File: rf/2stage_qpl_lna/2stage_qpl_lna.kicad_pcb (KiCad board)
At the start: 6 copper layers, 42 x 25 mm, 26 parts, among them J1 SMA, J2 EXT_PWR, J3 SMA, U1 QPL9547, U2 QPL9547, X1 SAW, X2 SAW

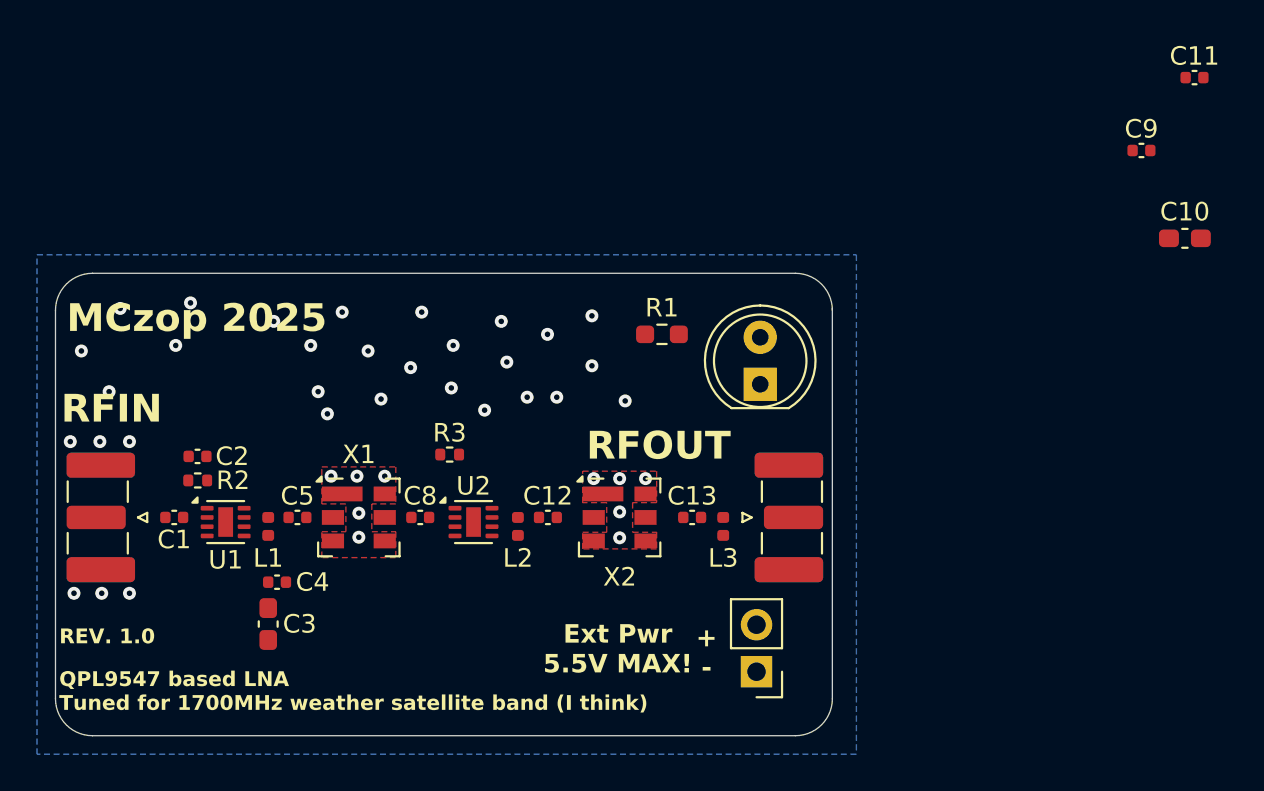
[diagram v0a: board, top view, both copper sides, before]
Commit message: Update QPL based LNA
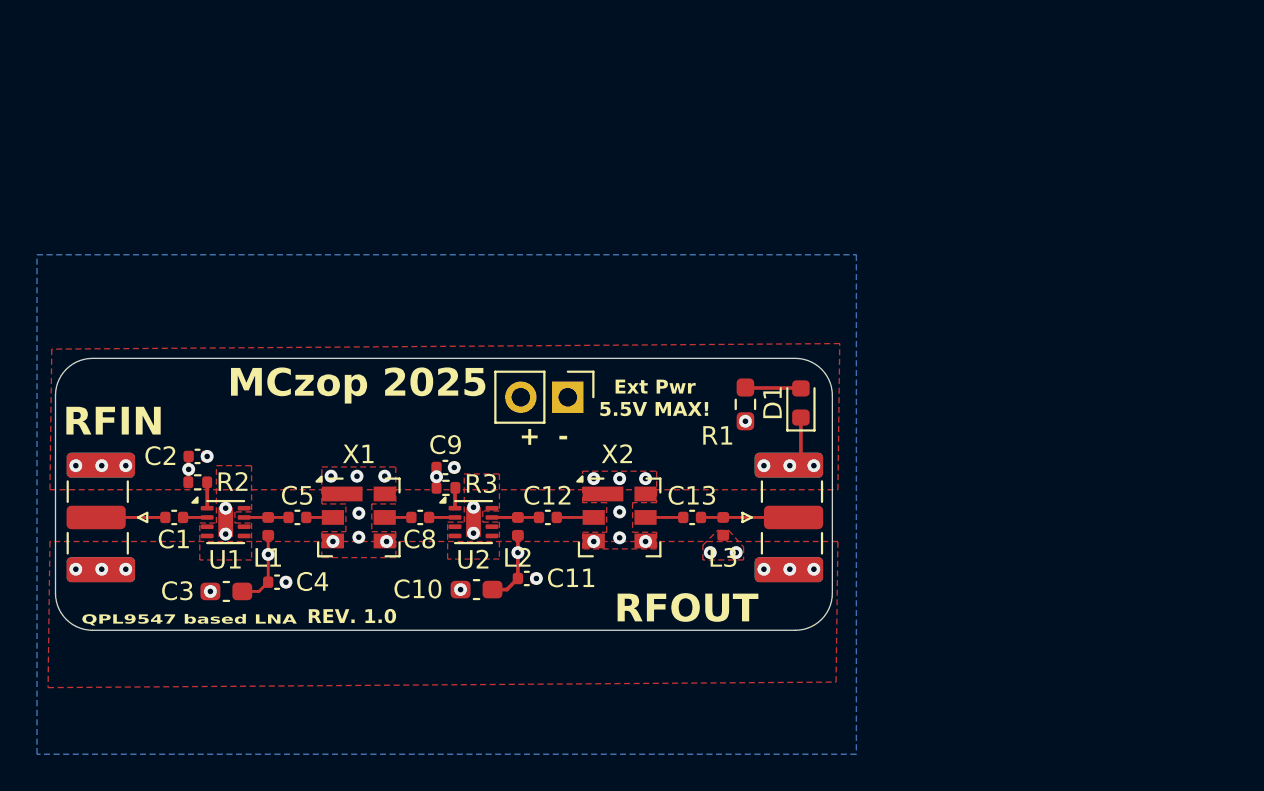
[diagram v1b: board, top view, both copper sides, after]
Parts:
- D1: footprint LED_THT:LED_D5.0mm_Clear -> LED_SMD:LED_0603_1608Metric
- moved C11 45.1 mm to (177.5, 106.5), turned to 180 degrees
- moved C10 42.7 mm to (174.8, 107.1), turned to 180 degrees
- moved C9 41.3 mm to (173.1, 100.5)
- moved J2 18.0 mm to (179.7, 96.7), turned to -90 degrees
- moved R1 5.89 mm to (189.3, 97.1), turned to 90 degrees
- moved C3 2.87 mm to (161.2, 107.2), turned to 180 degrees
- moved D1 2.42 mm to (192.3, 97.0)
- moved R3 1.81 mm to (173.1, 101.6)
- moved REF** 0.94 mm to (147.5, 105.4)
- moved R2 0.10 mm to (159.7, 101.3)
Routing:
- net VCC: track 0.00 -> 10.6 mm, vias 0 -> 7
- net Net-(J3-In): track 0.00 -> 5.00 mm
- net Net-(J1-In): track 0.00 -> 3.74 mm
- net Net-(D1-A): track 0.00 -> 3.11 mm
- net GND: track 0.00 -> 2.84 mm, vias 41 -> 36
- net Net-(C12-Pad1): track 0.00 -> 2.54 mm
- net Net-(C5-Pad1): track 0.00 -> 2.40 mm
- net Net-(X2-OUT): track 0.00 -> 2.04 mm
- net Net-(X2-IN): track 0.00 -> 2.00 mm
- net Net-(X1-OUT): track 0.00 -> 1.44 mm
- net Net-(X1-IN): track 0.00 -> 1.44 mm
- net Net-(U1-Vb): track 0.00 -> 1.40 mm
- net Net-(C8-Pad2): track 0.00 -> 1.40 mm
- net Net-(C1-Pad2): track 0.00 -> 1.30 mm
- net Net-(U2-Vb): track 0.00 -> 1.11 mm
- added copper zone on F.Cu, net VCC
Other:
- board size 42 x 25 mm -> 42 x 14.7 mm
- board text added: "QPL9547 based LNA"
- board text removed: "QPL9547 based LNA Tuned for 1700MHz weather satellite band (I think)"
